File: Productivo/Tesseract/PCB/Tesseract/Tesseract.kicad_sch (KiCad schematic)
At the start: 81 parts, among them J10 RTC, J11 READER, J13 PROG, J14 jumpers salida, J15 V-coil1, J16 V-coil2, J18 I2C, J18 RFW26, J19 Conn_01x06_Pin RTC, J19 OUT+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

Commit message: ajuste 2 capaz tesseract
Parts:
- D1: footprint Diode_SMD:D_MiniMELF_Handsoldering -> Diode_SMD:D_SOD-323_HandSoldering
- D10, D16, D3, D4, D5: footprint Diode_SMD:D_SOD-323 -> modelos:DIOM5336X320N
- D11, D12, D13, D14, D15, D18: footprint Diode_SMD:D_SMB -> modelos:DIOM5436X265N
- D17: footprint Diode_SMD:D_SOD-323 -> modelos:SOD3716X145N
- D6: footprint Diode_SMD:D_SMC_Handsoldering -> modelos:DIOM5336X320N
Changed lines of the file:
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@@
       (effects (font (size 1.27 1.27)))
     )
-    (property "Footprint" "Diode_SMD:D_SOD-323" (at 139.7 146.685 0)
+    (property "Footprint" "modelos:DIOM5336X320N" (at 139.7 146.685 0)
       (effects (font (size 1.27 1.27)) hide)
     )
@@
       (effects (font (size 1.27 1.27)) (justify left))
     )
-    (property "Footprint" "Diode_SMD:D_SMB" (at 25.4 138.43 0)
+    (property "Footprint" "modelos:DIOM5436X265N" (at 25.4 138.43 0)
       (effects (font (size 1.27 1.27)) hide)
     )
@@
       (effects (font (size 1.27 1.27)) (justify left))
     )
-    (property "Footprint" "Diode_SMD:D_SMB" (at 257.81 93.98 0)
+    (property "Footprint" "modelos:DIOM5436X265N" (at 257.81 93.98 0)
       (effects (font (size 1.27 1.27)) hide)
     )
@@
       (effects (font (size 1.27 1.27)) (justify left))
     )
-    (property "Footprint" "Diode_SMD:D_SMB" (at 64.77 130.81 0)
+    (property "Footprint" "modelos:DIOM5436X265N" (at 64.77 130.81 0)
       (effects (font (size 1.27 1.27)) hide)
     )
@@
       (effects (font (size 1.27 1.27)))
     )
-    (property "Footprint" "Diode_SMD:D_SMC_Handsoldering" (at 35.56 33.02 0)
+    (property "Footprint" "modelos:DIOM5336X320N" (at 35.56 33.02 0)
       (effects (font (size 1.27 1.27)) hide)
     )
@@
       (effects (font (size 1.27 1.27)) (justify left))
     )
-    (property "Footprint" "Diode_SMD:D_SMB" (at 52.07 133.35 0)
+    (property "Footprint" "modelos:DIOM5436X265N" (at 52.07 133.35 0)
       (effects (font (size 1.27 1.27)) hide)
     )
@@
       (effects (font (size 1.27 1.27)))
     )
-    (property "Footprint" "Diode_SMD:D_SOD-323" (at 247.65 93.345 0)
+    (property "Footprint" "modelos:SOD3716X145N" (at 247.65 93.345 0)
       (effects (font (size 1.27 1.27)) hide)
     )
@@
       (effects (font (size 1.27 1.27)))
     )
-    (property "Footprint" "Diode_SMD:D_SOD-323" (at 34.29 178.435 0)
+    (property "Footprint" "modelos:DIOM5336X320N" (at 34.29 178.435 0)
       (effects (font (size 1.27 1.27)) hide)
     )
@@
       (effects (font (size 1.27 1.27)))
     )
-    (property "Footprint" "Diode_SMD:D_SOD-323" (at 102.87 156.845 0)
+    (property "Footprint" "modelos:DIOM5336X320N" (at 102.87 156.845 0)
       (effects (font (size 1.27 1.27)) hide)
     )
@@
       (effects (font (size 1.27 1.27)) (justify left))
     )
-    (property "Footprint" "Diode_SMD:D_MiniMELF_Handsoldering" (at 215.9 40.64 0)
+    (property "Footprint" "Diode_SMD:D_SOD-323_HandSoldering" (at 215.9 40.64 0)
       (effects (font (size 1.27 1.27)) hide)
     )
@@
       (effects (font (size 1.27 1.27)) (justify left))
     )
-    (property "Footprint" "Diode_SMD:D_SMB" (at 38.1 135.89 0)
+    (property "Footprint" "modelos:DIOM5436X265N" (at 38.1 135.89 0)
       (effects (font (size 1.27 1.27)) hide)
     )
@@
       (effects (font (size 1.27 1.27)))
     )
-    (property "Footprint" "Diode_SMD:D_SOD-323" (at 146.05 156.845 0)
+    (property "Footprint" "modelos:DIOM5336X320N" (at 146.05 156.845 0)
       (effects (font (size 1.27 1.27)) hide)
     )
@@
       (effects (font (size 1.27 1.27)) (justify left))
     )
-    (property "Footprint" "Diode_SMD:D_SMB" (at 24.13 179.07 0)
+    (property "Footprint" "modelos:DIOM5436X265N" (at 24.13 179.07 0)
       (effects (font (size 1.27 1.27)) hide)
     )
@@
       (effects (font (size 1.27 1.27)))
     )
-    (property "Footprint" "Diode_SMD:D_SOD-323" (at 95.25 146.685 0)
-      (effects (font (size 1.27 1.27)) hide)
-    )
+    (property "Footprint" "modelos:DIOM5336X320N" (at 95.25 146.685 0)
+      (effects (font (size 1.27 1.27)) hide)
+    )

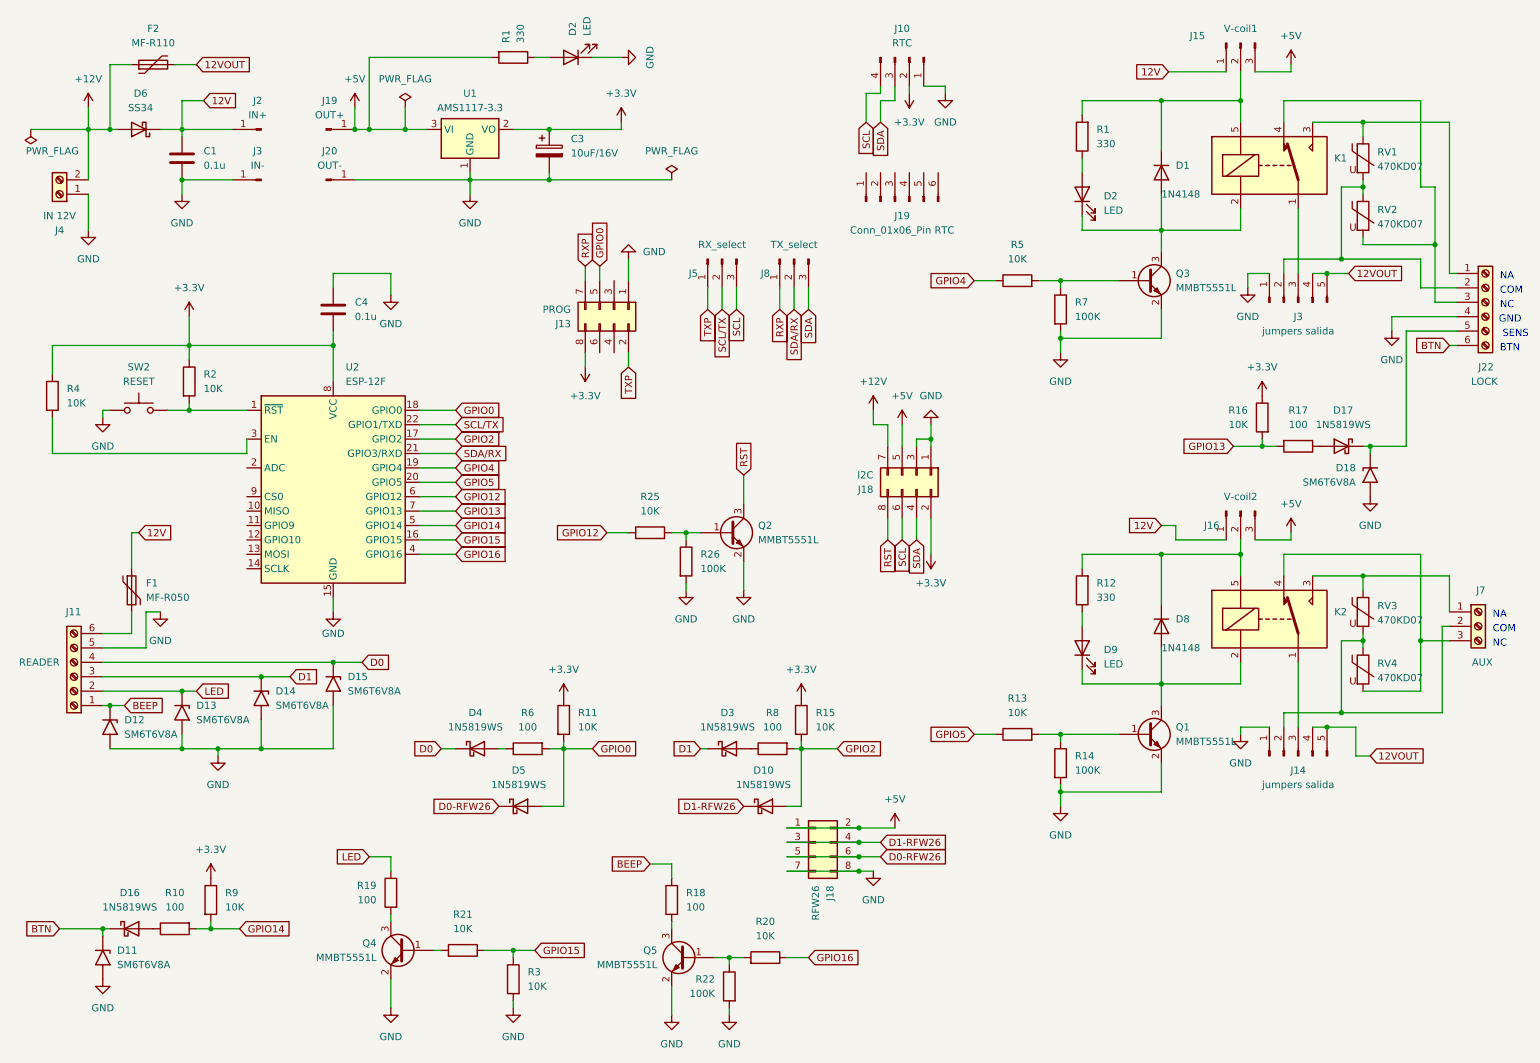
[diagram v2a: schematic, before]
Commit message: agregado de Fuente a tesseract
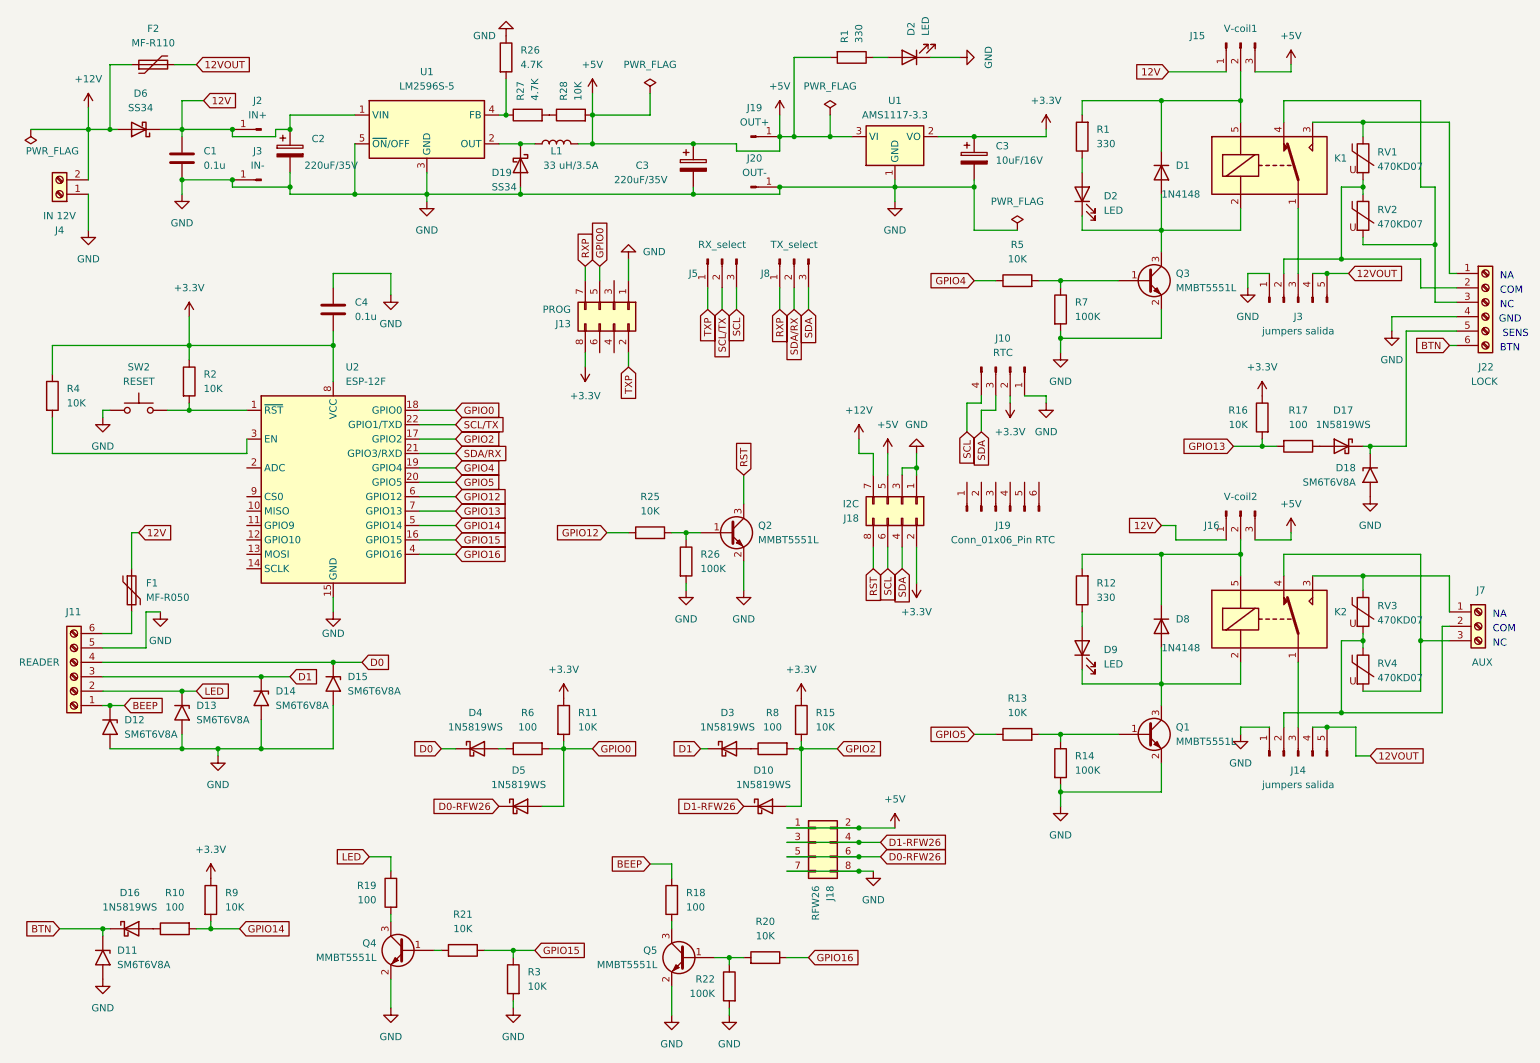
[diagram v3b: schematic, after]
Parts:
- added C2, C3: 220uF/35V, Capacitor_SMD:CP_Elec_8x10, symbol Device:C_Polarized
- added D19: SS34, Diode_SMD:D_SMC_Handsoldering, symbol Device:D_Schottky
- added L1: 33 uH/3.5A, Inductor_SMD:L_12x12mm_H8mm, symbol Device:L
- added R26, R27: 4.7K, Resistor_SMD:R_1206_3216Metric_Pad1.30x1.75mm_HandSolder, symbol Device:R
- added R28: 10K, Resistor_SMD:R_1206_3216Metric_Pad1.30x1.75mm_HandSolder, symbol Device:R
- added U1: LM2596S-5, Package_TO_SOT_THT:TO-220-5_Vertical, symbol Regulator_Switching:LM2596S-5
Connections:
- net +5V: now also C3.1, L1.2, R28.2
- net 12V: now also C2.1, U1.1 (VIN)
- net GND: now also C2.2, C3.2, D19.2 (A), R26.1, U1.3 (GND), U1.5 (~{ON}/OFF)
- new net: R26.2, R27.1, U1.4 (FB)
- new net: R27.2, R28.1
- new net: D19.1 (K), L1.1, U1.2 (OUT)
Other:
- moved on the sheet: C3, D2, J10, J18, J19, J20, R1, U1

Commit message: reacomodado de componentes
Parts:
- C2, C3: footprint Capacitor_SMD:CP_Elec_8x10 -> Capacitor_SMD:CP_Elec_10x10
- D10, D16, D3, D4, D5: footprint modelos:DIOM5336X320N -> modelos:SOD3716X145N
- D19: footprint Diode_SMD:D_SMC_Handsoldering -> modelos:DIOM5336X320N
- D8: footprint Diode_SMD:D_MiniMELF_Handsoldering -> Diode_SMD:D_SOD-323_HandSoldering
- U1: footprint Package_TO_SOT_THT:TO-220-5_Vertical -> Package_TO_SOT_THT:TO-220-5_P3.4x3.7mm_StaggerOdd_Lead3.8mm_Vertical
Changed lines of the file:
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@@
       (effects (font (size 1.27 1.27)))
     )
-    (property "Footprint" "modelos:DIOM5336X320N" (at 139.7 146.685 0)
+    (property "Footprint" "modelos:SOD3716X145N" (at 139.7 146.685 0)
       (effects (font (size 1.27 1.27)) hide)
     )
@@
       (effects (font (size 1.27 1.27)) (justify left))
     )
-    (property "Footprint" "Capacitor_SMD:CP_Elec_8x10" (at 63.1952 40.64 0)
+    (property "Footprint" "Capacitor_SMD:CP_Elec_10x10" (at 63.1952 40.64 0)
       (effects (font (size 1.27 1.27)) hide)
     )
@@
       (effects (font (size 1.27 1.27)) (justify left))
     )
-    (property "Footprint" "Diode_SMD:D_MiniMELF_Handsoldering" (at 215.9 120.65 0)
+    (property "Footprint" "Diode_SMD:D_SOD-323_HandSoldering" (at 215.9 120.65 0)
       (effects (font (size 1.27 1.27)) hide)
     )
@@
       (effects (font (size 1.27 1.27)))
     )
-    (property "Footprint" "modelos:DIOM5336X320N" (at 34.29 178.435 0)
+    (property "Footprint" "modelos:SOD3716X145N" (at 34.29 178.435 0)
       (effects (font (size 1.27 1.27)) hide)
     )
@@
       (effects (font (size 1.27 1.27)))
     )
-    (property "Footprint" "modelos:DIOM5336X320N" (at 102.87 156.845 0)
+    (property "Footprint" "modelos:SOD3716X145N" (at 102.87 156.845 0)
       (effects (font (size 1.27 1.27)) hide)
     )
@@
       (effects (font (size 1.27 1.27)) (justify left))
     )
-    (property "Footprint" "Capacitor_SMD:CP_Elec_8x10" (at 134.3152 43.18 0)
+    (property "Footprint" "Capacitor_SMD:CP_Elec_10x10" (at 134.3152 43.18 0)
       (effects (font (size 1.27 1.27)) hide)
     )
@@
       (effects (font (size 1.27 1.27)))
     )
-    (property "Footprint" "modelos:DIOM5336X320N" (at 146.05 156.845 0)
+    (property "Footprint" "modelos:SOD3716X145N" (at 146.05 156.845 0)
       (effects (font (size 1.27 1.27)) hide)
     )
@@
       (effects (font (size 1.27 1.27)))
     )
-    (property "Footprint" "modelos:DIOM5336X320N" (at 95.25 146.685 0)
+    (property "Footprint" "modelos:SOD3716X145N" (at 95.25 146.685 0)
       (effects (font (size 1.27 1.27)) hide)
     )
@@
       (effects (font (size 1.27 1.27)) (justify left))
     )
-    (property "Footprint" "Diode_SMD:D_SMC_Handsoldering" (at 102.87 39.37 0)
+    (property "Footprint" "modelos:DIOM5336X320N" (at 102.87 39.37 0)
       (effects (font (size 1.27 1.27)) hide)
     )
@@
       (effects (font (size 1.27 1.27)))
     )
-    (property "Footprint" "Package_TO_SOT_THT:TO-220-5_Vertical" (at 87.63 39.37 0)
+    (property "Footprint" "Package_TO_SOT_THT:TO-220-5_P3.4x3.7mm_StaggerOdd_Lead3.8mm_Vertical" (at 87.63 39.37 0)
       (effects (font (size 1.27 1.27) italic) (justify left) hide)
     )
